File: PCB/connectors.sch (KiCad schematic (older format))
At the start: 54 parts

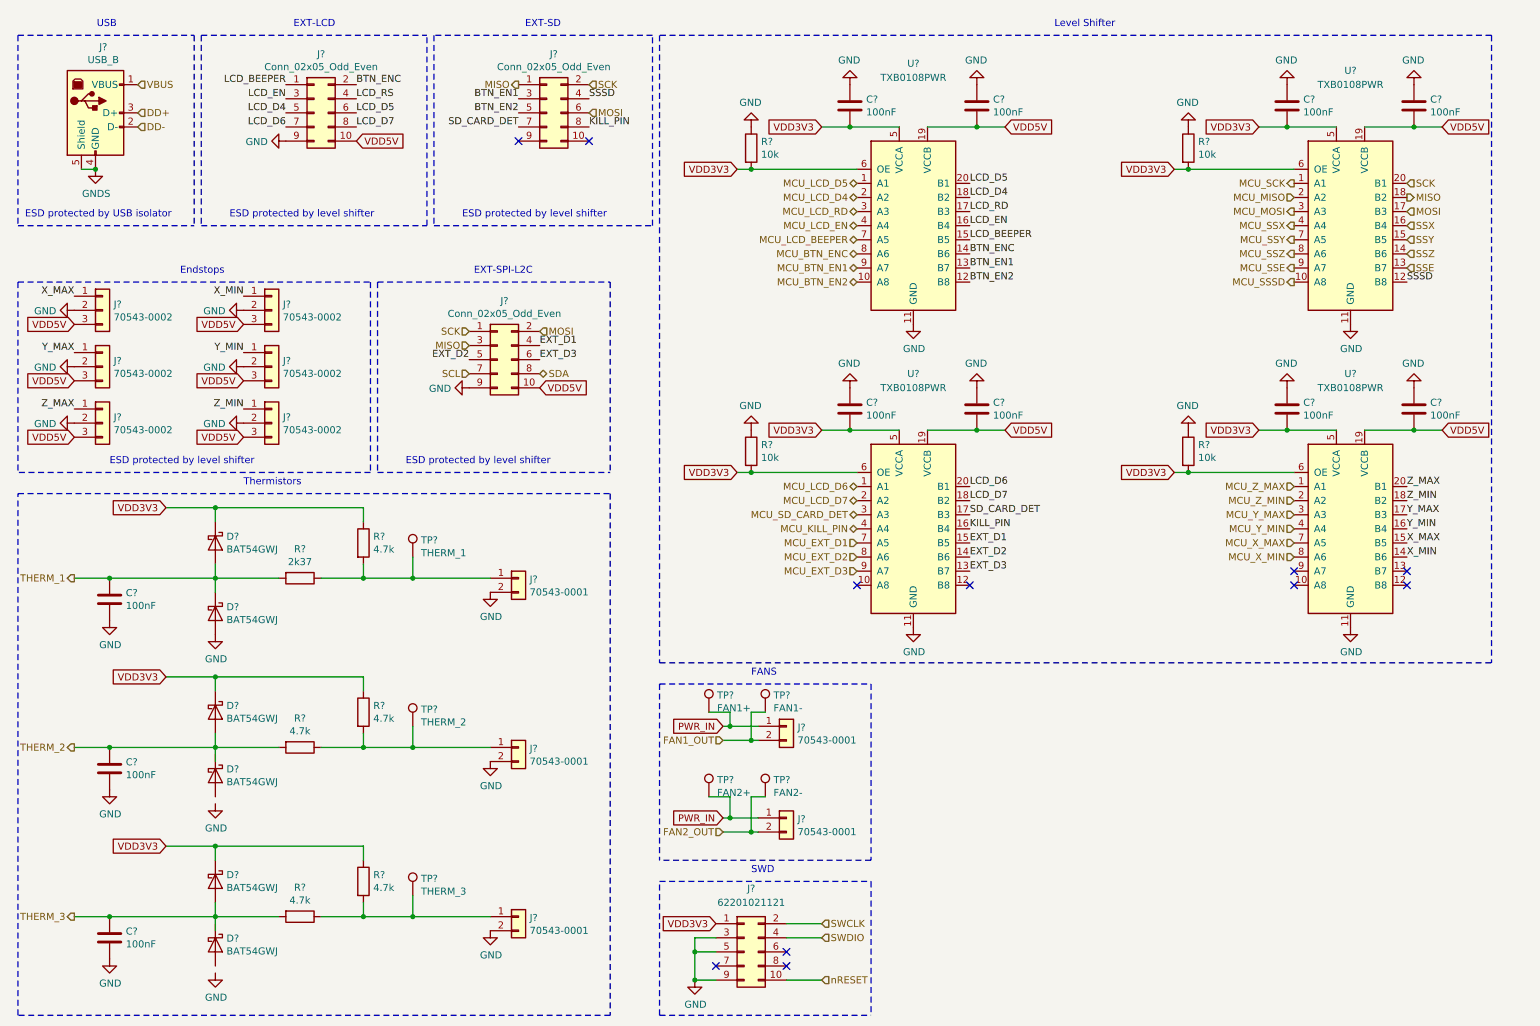
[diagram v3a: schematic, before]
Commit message: Fixed bugs found with ERC.
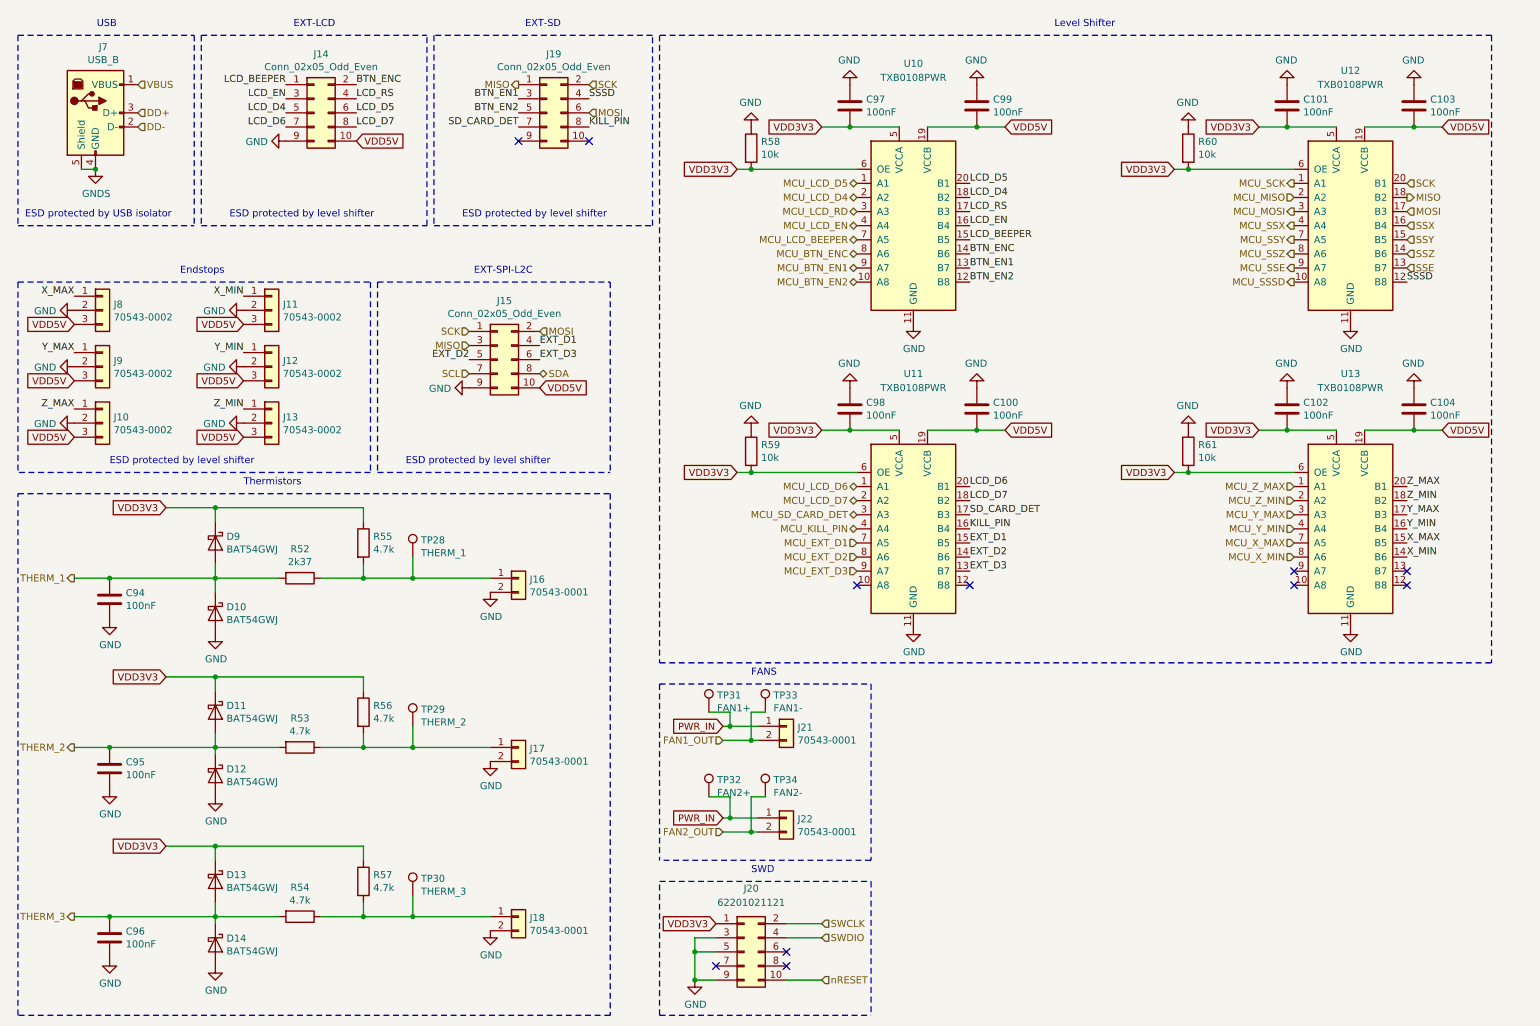
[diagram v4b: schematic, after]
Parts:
- gave numbers to parts that had none: 54
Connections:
- net LCD_RD is gone; now on net LCD_RS: U10.17 (B3)
- net GND: now also D12.2 (A), D14.2 (A)
- net THERM_2: now also D12.1 (K)
- net THERM_3: now also D14.1 (K)

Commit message: Added missing foorprints.
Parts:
- C94, C95, C96: footprint (none) -> Capacitor_SMD:C_0603_1608Metric
- J7: footprint (none) -> Connector_USB:USB_B_TE_5787834_Vertical
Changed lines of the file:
@@
 F 0 "J7" H 1205 1767 50  0000 C CNN
 F 1 "USB_B" H 1205 1676 50  0000 C CNN
-F 2 "" H 1300 1250 50  0001 C CNN
-F 3 "" H 1300 1250 50  0001 C CNN
+F 2 "Connector_USB:USB_B_TE_5787834_Vertical" H 1300 1250 50  0001 C CNN
+F 3 "https://www.mouser.de/ProductDetail/TE-Connectivity/5787834-1?qs=sGAEpiMZZMulM8LPOQ%252bykzAp4yt8IxVbCJriWtalJzg%3d" H 1300 1250 50  0001 C CNN
 	1    1150 1300
 	1    0    0    -1
@@
 F 0 "C94" H 1365 4796 50  0000 L CNN
 F 1 "100nF" H 1365 4705 50  0000 L CNN
-F 2 "" H 1288 4600 50  0001 C CNN
+F 2 "Capacitor_SMD:C_0603_1608Metric" H 1288 4600 50  0001 C CNN
 F 3 "~" H 1250 4750 50  0001 C CNN
 	1    1250 4750
@@
 F 0 "C95" H 1365 5996 50  0000 L CNN
 F 1 "100nF" H 1365 5905 50  0000 L CNN
-F 2 "" H 1288 5800 50  0001 C CNN
+F 2 "Capacitor_SMD:C_0603_1608Metric" H 1288 5800 50  0001 C CNN
 F 3 "~" H 1250 5950 50  0001 C CNN
 	1    1250 5950
@@
 F 0 "C96" H 1365 7196 50  0000 L CNN
 F 1 "100nF" H 1365 7105 50  0000 L CNN
-F 2 "" H 1288 7000 50  0001 C CNN
+F 2 "Capacitor_SMD:C_0603_1608Metric" H 1288 7000 50  0001 C CNN
 F 3 "~" H 1250 7150 50  0001 C CNN
 	1    1250 7150

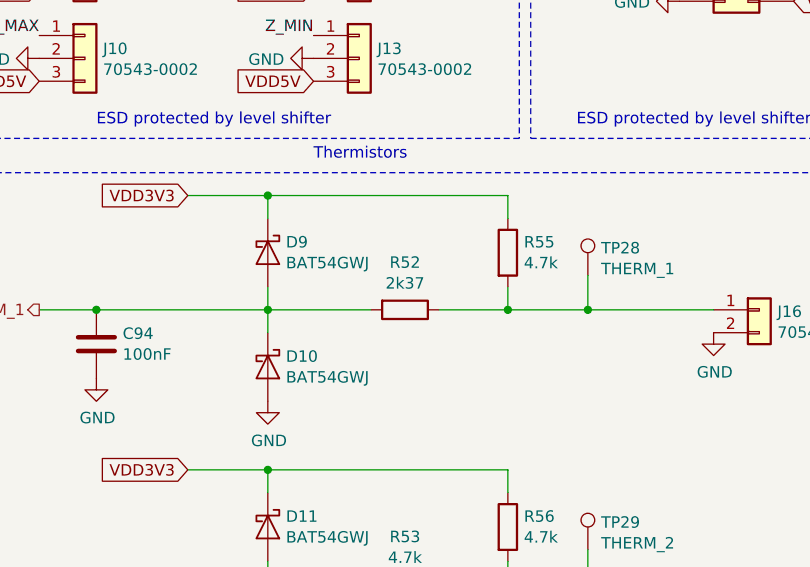
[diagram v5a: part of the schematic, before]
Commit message: Fixed annotations and assignment errors.
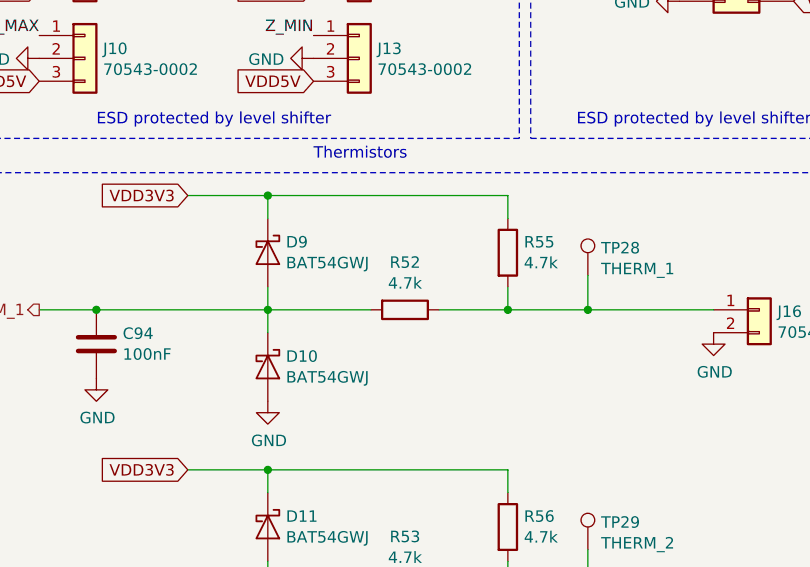
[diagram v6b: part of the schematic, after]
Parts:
- R52: value 2k37 -> 4.7k
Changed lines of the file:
@@
 P 2600 4600
 F 0 "R52" V 2393 4600 50  0000 C CNN
-F 1 "2k37" V 2484 4600 50  0000 C CNN
+F 1 "4.7k" V 2484 4600 50  0000 C CNN
 F 2 "Resistor_SMD:R_0603_1608Metric" V 2530 4600 50  0001 C CNN
 F 3 "~" H 2600 4600 50  0001 C CNN
